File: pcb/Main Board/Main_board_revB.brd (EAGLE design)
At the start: 49.2 x 85.1 mm, 11 parts

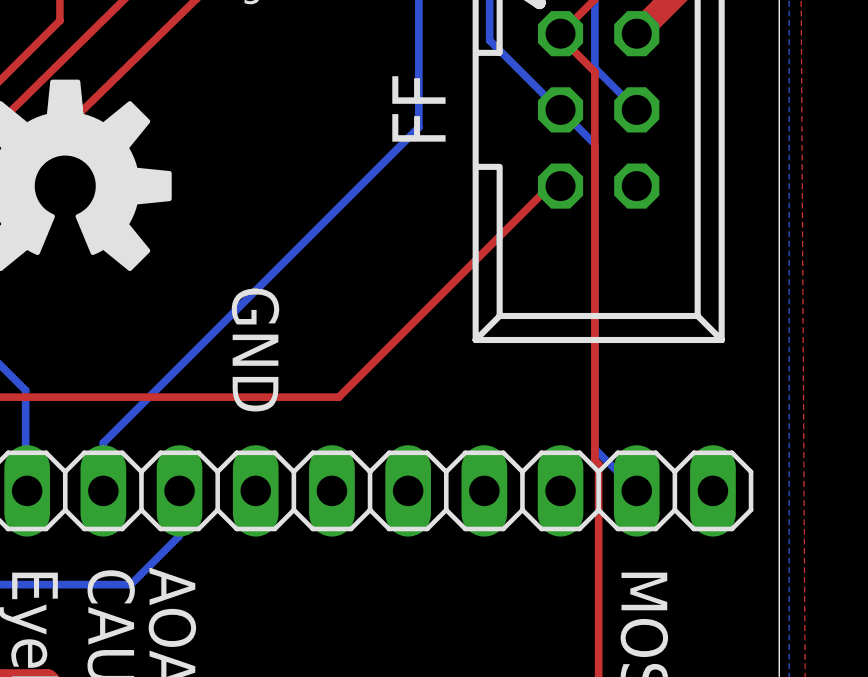
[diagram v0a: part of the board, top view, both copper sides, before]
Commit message: fixes for Main board design, added pdf schematic for the screen adapter
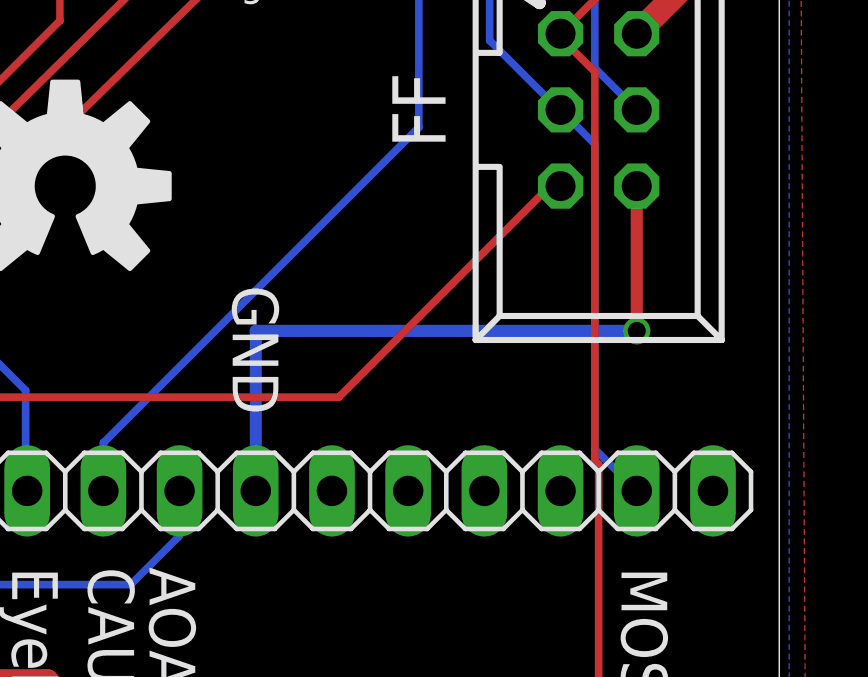
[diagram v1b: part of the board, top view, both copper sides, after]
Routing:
- net GND: track 26.2 -> 49.0 mm, vias 2 -> 3
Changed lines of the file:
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@@
 <wire x1="24.384" y1="57.3786" x2="37.0332" y2="57.3786" width="0.254" layer="1"/>
 <wire x1="24.1554" y1="57.6072" x2="24.384" y2="57.3786" width="0.254" layer="1"/>
-<wire x1="39.5478" y1="51.816" x2="39.5478" y2="50.9778" width="0" layer="19" extent="1-16"/>
 <wire x1="39.5478" y1="50.9778" x2="39.5478" y2="37.8714" width="0.254" layer="16"/>
 <wire x1="41.8338" y1="35.5854" x2="41.91" y2="35.56" width="0.254" layer="16"/>
@@
 <via x="34.036" y="62.23" extent="1-16" drill="0.7"/>
 <wire x1="27.94" y1="62.23" x2="34.036" y2="62.23" width="0.8128" layer="1"/>
-<wire x1="44.45" y1="33.02" x2="31.75" y2="22.86" width="0" layer="19" extent="1-1"/>
+<wire x1="44.45" y1="33.02" x2="44.45" y2="28.194" width="0.4064" layer="1"/>
+<via x="44.45" y="28.194" extent="1-16" drill="0.6" shape="square"/>
+<wire x1="44.45" y1="28.194" x2="31.75" y2="28.194" width="0.4064" layer="16"/>
+<wire x1="31.75" y1="28.194" x2="31.75" y2="22.86" width="0.4064" layer="16"/>
 </signal>
 <signal name="+5V" class="1">
